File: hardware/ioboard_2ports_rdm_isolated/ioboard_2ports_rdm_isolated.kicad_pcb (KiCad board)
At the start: 2 copper layers, 106 x 55 mm, 32 parts, among them J1 Conn_02x06_Odd_Even, J12 Conn_01x03, J2 XLR3, J3 XLR3, J4 8P8C, J5 8P8C, J6 Conn_01x03, J8 XLR3, J9 XLR3, U1 M24C64-RMN6TP, U2 CRE1S0505DC, U4 ADM2483xRW, U6 ADM2483xRW

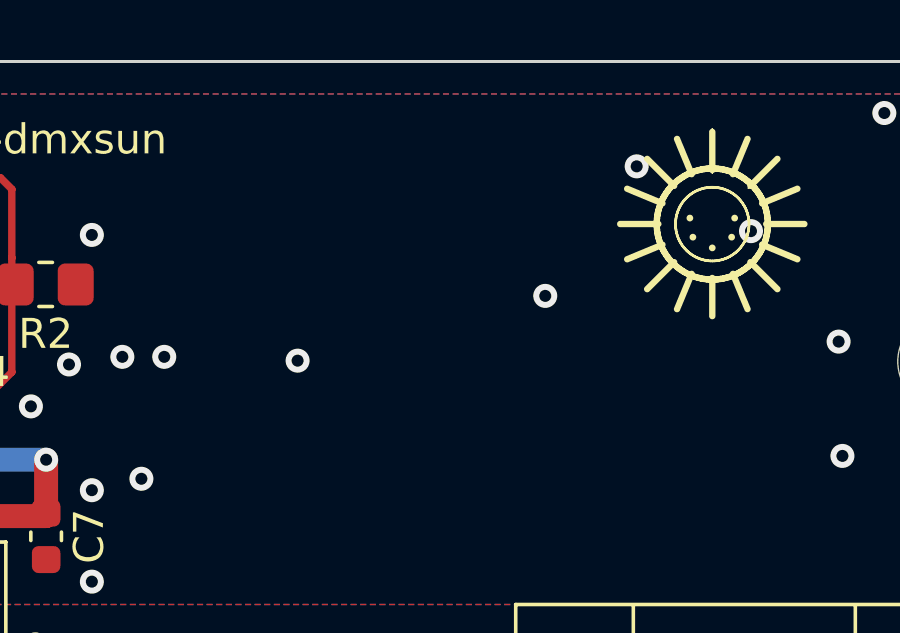
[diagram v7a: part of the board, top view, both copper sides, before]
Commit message: Update ioboards to KiCad 8, add OpenHardware logo
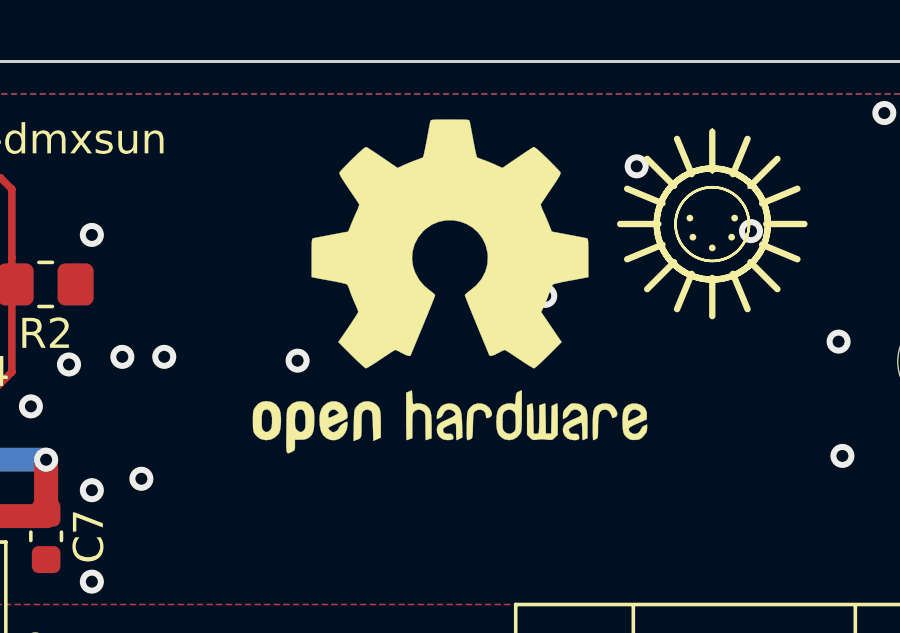
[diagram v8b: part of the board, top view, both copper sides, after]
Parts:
- added SYM1: Logo_Open_Hardware_Large, Symbol:OSHW-Logo2_14.6x12mm_SilkScreen, F.Cu at (109.5, 27.5)
